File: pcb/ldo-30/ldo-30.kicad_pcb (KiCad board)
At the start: 2 copper layers, 20 x 17.5 mm, 11 parts, among them IC1 TP4056, J1 BATT, J2 buck-boost-conn, J3 PWR, U1 XC6220

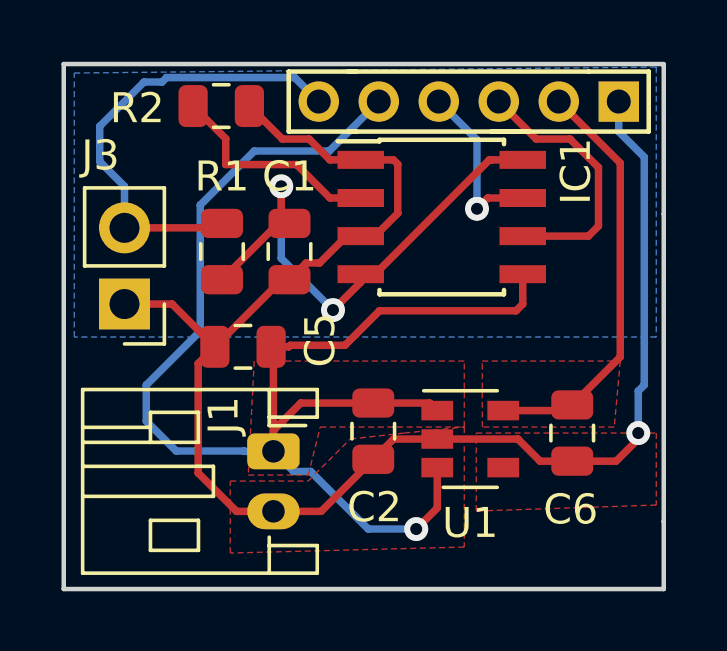
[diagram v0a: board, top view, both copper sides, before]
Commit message: updated footprint
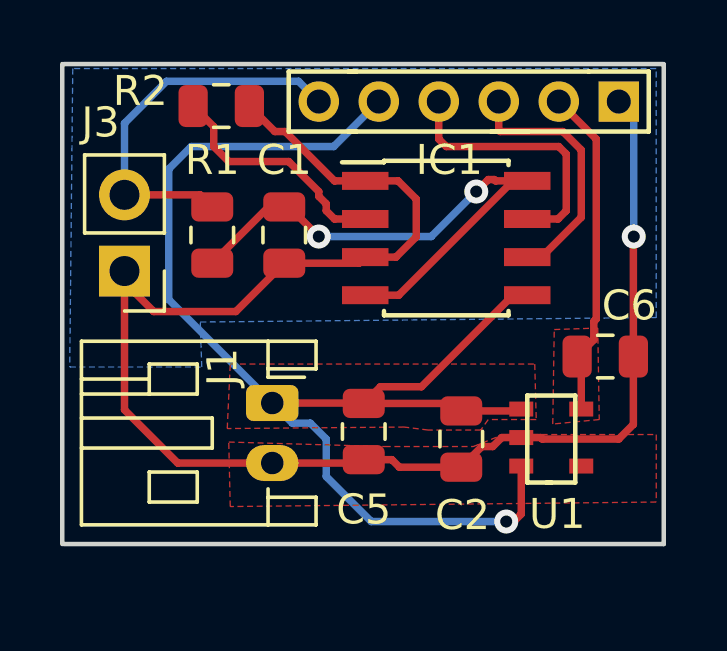
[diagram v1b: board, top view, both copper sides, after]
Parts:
- U1: footprint Package_TO_SOT_SMD:SOT-23-5 -> xc6220:XC6220
- moved C5 4.92 mm to (99.2, 85.8), turned to 270 degrees
- moved C2 2.94 mm to (102.5, 86.0)
- moved C6 2.78 mm to (107.3, 83.2), turned to 180 degrees
- moved U1 2.70 mm to (105.5, 86.0), turned to 270 degrees
- moved J1 1.61 mm to (96.2, 84.8)
- moved J3 1.10 mm to (91.3, 80.4)
- moved IC1 0.72 mm to (102.0, 79.3)
- moved R1 0.64 mm to (94.2, 79.2)
- moved C1 0.58 mm to (96.6, 79.2)
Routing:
- net BATT: track 48.3 -> 44.9 mm
- net CHRG: track 5.78 -> 9.01 mm, vias 1 -> 0
- net /3.0V: track 14.1 -> 11.1 mm
- net +5V: track 15.3 -> 12.8 mm
- net GND: track 51.9 -> 53.7 mm
- net Net-(C1-Pad1): track 17.8 -> 19.5 mm
- net Net-(IC1-Pad2): track 7.36 -> 7.91 mm
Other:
- board size 20 x 17.5 mm -> 20 x 16 mm
